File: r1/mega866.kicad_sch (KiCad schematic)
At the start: 18 parts, among them J1 ZSM1-SM1, J2 ZSM1-SM2

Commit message: schematic draft
Signed-off-by: John McMaster <johndmcmaster@gmail.com>
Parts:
- removed J? (x5): tl866_dip40, symbol mega866:tl866_dip40
- removed R?: 100k, Resistor_SMD:R_0603_1608Metric, symbol Device:R
- added J? (x4): tl866_dip40, symbol mega866:tl866_dip40
- added J? (x2): Conn_01x02_Male, symbol Connector:Conn_01x02_Male
- added Q? (x2): 2N7002, Package_TO_SOT_SMD:SOT-23, symbol Transistor_FET:2N7002
- added Q?: BSS84, Package_TO_SOT_SMD:SOT-23, symbol Transistor_FET:IRF7606PBF
- added R? (x4): NOLOAD, Resistor_SMD:R_0603_1608Metric, symbol Device:R
- added R? (x10): 0, Resistor_SMD:R_0603_1608Metric, symbol Device:R
- added R? (x3): 4.7k, Resistor_SMD:R_0603_1608Metric, symbol Device:R
- added R?: 100k, Resistor_SMD:R_0603_1608Metric, symbol Device:R
- added R? (x2): 47k, Resistor_SMD:R_0603_1608Metric, symbol Device:R
- added U?: Pico, MCU_RaspberryPi_and_Boards:RPi_Pico_SMD_TH, symbol MCU_RaspberryPi_and_Boards:Pico
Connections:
- net BPM_SR_CLK: now also U?.20 (GPIO15)
- net BPM_SR_D: now also U?.19 (GPIO14)
- net G001: now also J?.1
- net G002: now also J?.21
- net G003: now also J?.40
- net G004: now also J?.20
- net G005: now also J?.2
- net G006: now also J?.22
- net G007: now also J?.39
- net G008: now also J?.19
- net G009: now also J?.3
- net G010: now also J?.23
- net G011: now also J?.38
- net G012: now also J?.18
- net G013: now also J?.4
- net G014: now also J?.24
- net G015: now also J?.37
- net G016: now also J?.17
- net G017: now also J?.5
- net G018: now also J?.25
- net G019: now also J?.36
- net G020: now also J?.16
- net G021: now also J?.6
- net G022: now also J?.26
- net G023: now also J?.35
- net G024: now also J?.15
- net G025: now also J?.7
- net G026: now also J?.27
- net G027: now also J?.34
- net G028: now also J?.14
- net G029: now also J?.8
- net G030: now also J?.28
- net G031: now also J?.33
- net G032: now also J?.13
- net G033: now also J?.9, R?.1
- net G034: now also J?.29
- net G035: now also J?.32
- net G036: now also J?.12
- net G037: now also J?.10, R?.1
- net G038: now also J?.30
- net G039: now also J?.31, R?.1
- net G040: now also J?.11
- net G041: now also J?.11, R?.1
- net G042: now also J?.31
- net G043: now also J?.30, Q?.3 (D), R?.1
- net G044: now also J?.10
- net G045: now also J?.12, R?.1
- net G046: now also J?.32
- net G047: now also J?.29
- net G048: now also J?.9
- net G049: now also J?.13
- net G050: now also J?.33
- net G051: now also J?.28
- net G052: now also J?.8
- net G053: now also J?.14
- net G054: now also J?.34
- net G055: now also J?.27
- net G056: now also J?.7
- net G057: now also J?.15
- net G058: now also J?.35
- net G059: now also J?.26
- net G060: now also J?.6
- net G061: now also J?.16
- net G062: now also J?.36
- net G063: now also J?.25
- net G064: now also J?.5
- net G065: now also J?.17
- net G066: now also J?.37
- net G067: now also J?.24
- net G068: now also J?.4
- net G069: now also J?.18
- net G070: now also J?.38
- net G071: now also J?.23
- net G072: now also J?.3
- net G073: now also J?.19
- net G074: now also J?.39
- net G075: now also J?.22
- net G076: now also J?.2
- net G077: now also J?.20
- net G078: now also J?.40
- net G079: now also J?.21
- net G080: now also J?.1
- net G081: now also J?.1
- net G082: now also J?.21
- net G083: now also J?.40
- net G084: now also J?.20
- net G085: now also J?.2
- net G086: now also J?.22
- net G087: now also J?.39
- net G088: now also J?.19
- net G089: now also J?.3
- net G090: now also J?.23
- net G091: now also J?.38
- net G092: now also J?.18
- net G093: now also J?.4
- net G094: now also J?.24
- net G095: now also J?.37
- net G096: now also J?.17
- net G097: now also J?.5
- net G098: now also J?.25
- net G099: now also J?.36
- net G100: now also J?.16
- net G101: now also J?.6
- net G102: now also J?.26
- net G103: now also J?.35
- net G104: now also J?.15
- net G105: now also J?.7
- net G106: now also J?.27
- net G107: now also J?.34
- net G108: now also J?.14
- net G109: now also J?.8
- net G110: now also J?.28
- net G111: now also J?.33
- net G112: now also J?.13
- net G113: now also J?.9
- net G114: now also J?.29
- net G115: now also J?.32
- net G116: now also J?.12
- net G117: now also J?.10
- net G118: now also J?.30
- net G119: now also J?.31
- net G120: now also J?.11
- net G121: now also J?.11
- net G122: now also J?.31
- net G123: now also J?.30
- net G124: now also J?.10
- net G125: now also J?.12
- net G126: now also J?.32
- net G127: now also J?.29
- net G128: now also J?.9
- net G129: now also J?.13
- net G130: now also J?.33
- net G131: now also J?.28
- net G132: now also J?.8
- net G133: now also J?.14
- net G134: now also J?.34
- net G135: now also J?.27
- net G136: now also J?.7
- net G137: now also J?.15
- net G138: now also J?.35
- net G139: now also J?.26
- net G140: now also J?.6
- net G141: now also J?.16
- net G142: now also J?.36
- net G143: now also J?.25
- net G144: now also J?.5
- net G145: now also J?.17
- net G146: now also J?.37
- net G147: now also J?.24
- net G148: now also J?.4
- net G149: now also J?.18
- net G150: now also J?.38
- net G151: now also J?.23
- net G152: now also J?.3
- net G153: now also J?.19
- net G154: now also J?.39
- net G155: now also J?.22
- net G156: now also J?.2
- net G157: now also J?.20
- net G158: now also J?.40
- net G159: now also J?.21
- net G160: now also J?.1
- net GND: now also Q?.2 (S), Q?.2 (S), R?.1, R?.1, R?.2, U?.13 (GND), U?.18 (GND), U?.23 (GND), U?.28 (GND), U?.3 (GND), U?.33 (AGND), U?.38 (GND), U?.8 (GND)
- net LED1: now also U?.21 (GPIO16)
- net LED2: now also U?.22 (GPIO17)
- net SM_DET: now also R?.2, U?.24 (GPIO18)
- net VCC: now also J?.2 (Pin_2), U?.39 (VSYS)
- net SM2_C3: now reaches J2.C3 (RFU)
- net SM2_C3: now also R?.1
- net COILP: now reaches J2.C4 (RFU)
- net COILP: now also Q?.5 (D), Q?.6 (D), Q?.7 (D), Q?.8 (D)
- net at J1.C3 (I2C_SDA): now also R?.2, R?.2
- net at J1.C4 (I2C_SCL): now also R?.1, R?.1
- net SM1_C5: now reaches J1.C5 (RFU)
- net SM1_C5: now also R?.1
- net P2R: now reaches J1.A30 (RFU)
- net P2R: now also J?.1 (Pin_1)
- net SM2_A5: now reaches J2.A5 (RFU)
- net SM2_A5: now also R?.1
- new net: R?.2, U?.31 (GPIO26_ADC0)
- new net: R?.2, U?.29 (GPIO22)
- new net: R?.2, U?.27 (GPIO21)
- new net: Q?.3 (D), Q?.4 (G), R?.1
- new net: J?.1 (Pin_1), Q?.1 (S), Q?.2 (S), Q?.3 (S), R?.2
- new net +3V3: R?.1, R?.1
- new net COIL_EN: Q?.1 (G), Q?.1 (G), R?.2, U?.25 (GPIO19)
- new net COIL_GPIO: J?.2 (Pin_2), U?.26 (GPIO20)
- new net EEPROM CLK: U?.4 (GPIO2)
- new net EEPROM CS: R?.1, U?.2 (GPIO1)
- new net EEPROM DI: U?.5 (GPIO3)
- new net EEPROM DO: U?.1 (GPIO0)
- new net G033_GPIO: R?.2, U?.9 (GPIO6)
- new net G037_GPIO: R?.2, U?.10 (GPIO7)
- new net G039_GPIO: R?.2, U?.11 (GPIO8)
- new net G041_GPIO: R?.2, U?.12 (GPIO9)
- new net G043_GPIO: R?.2, U?.14 (GPIO10)
- new net G045_GPIO: R?.2, U?.15 (GPIO11)
- new net I2C SCL: R?.1, R?.2, U?.7 (GPIO5)
- new net I2C SDA: R?.2, R?.2, U?.6 (GPIO4)
- new net SM2_C5: R?.1
- new net UART1: R?.2, U?.16 (GPIO12)
- new net UART2: R?.1, U?.17 (GPIO13)
- no-connect marks 10 -> 9
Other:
- note added: "3.3V to 5V level translation"
- note added: "A7 COILN"
- note added: "Although we could just switch COILN, don't apply power until we have a compatible connection"
- note added: "Considered TL866 for misc GPIO, but use RP2040 since easier to get and consistent with zscn"
- note added: "Following pins were connected on SM48D: -SM2.A12 (G033): G015 -SM2.A10 (G037): G019 -SM2.A09 (G039): G023 -SM2.A08 (G041): G027 Provide a way to test connections Add a few extra in case more are used that I don't know about"
- note added: "Give some flexibility for other voltage Bridge / jumper if unused"
- note added: "RFU: UART"
- note added: "SM48D relay control When COIL_EN is asserted, the SM will connect P2R to P2 Right circuit drives relay COILP (SM2.C4) Note COILN on G043 (SM2.A7) Add transistor here to make atomic, although we could probably toggle through TL866"
- note added: "Signal fed into SM's relay When closed, connects to P2 Intended for loopback testing?"
- note removed: "93C46B"
- note removed: "Misc GPIO w/ tl866 to keep things consistent? Otherwise rp2040"
- note removed: "VCC 3.3V or 5V probably ok"
- moved on the sheet: D?, J1A, J1B, J1C, J2A, J2B, J2C, R?

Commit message: fix erc errors
Signed-off-by: John McMaster <johndmcmaster@gmail.com>
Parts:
- removed J?: Conn_01x06_Male, symbol Connector:Conn_01x06_Male
- removed R?: 4.7k, Resistor_SMD:R_0603_1608Metric, symbol Device:R
- removed R?: 0, Resistor_SMD:R_0603_1608Metric, symbol Device:R
- added R4: 4.7k, Resistor_SMD:R_0603_1608Metric, symbol Device:R
- gave numbers to parts that had none: 37
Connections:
- net +3V3: now also R4.1
- net I2C SCL: now also R4.2
- no-connect marks 9 -> 31

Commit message: cleaner drc / fix errors
Signed-off-by: John McMaster <johndmcmaster@gmail.com>
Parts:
- D1, D2: footprint (none) -> LED_SMD:LED_0603_1608Metric
- J1: footprint zsm:5650470-5 -> TE_5650933-5; symbol zsm:ZSM1-SM1 -> mega866:ZSM1-SM1
- J10, J6, J7, J9: footprint (none) -> Connector_PinHeader_2.54mm:PinHeader_1x06_P2.54mm_Vertical
- J2: symbol zsm:ZSM1-SM2 -> mega866:ZSM1-SM2
- J5, J8: footprint (none) -> Connector_PinHeader_2.54mm:PinHeader_1x02_P2.54mm_Vertical
- R1, R2: footprint (none) -> Resistor_SMD:R_0603_1608Metric
- U1: footprint MCU_RaspberryPi_and_Boards:RPi_Pico_SMD_TH -> mega866:RPi_Pico_SMD_TH; symbol MCU_RaspberryPi_and_Boards:Pico -> mega866:Pico
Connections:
- net EE_CLK is gone; now on net EEPROM_CLK: J2.A3 (EE_CLK)
- net EE_CS is gone; now on net EEPROM_CS: J2.A4 (EE_CS)
- net EE_DI is gone; now on net EEPROM_DI: J2.A2 (EE_DI)
- net EE_DO is gone; now on net EEPROM_DO: J2.A1 (EE_DO)
- net EEPROM CLK renamed EEPROM_CLK
- net EEPROM CS renamed EEPROM_CS
- net EEPROM DI renamed EEPROM_DI
- net EEPROM DO renamed EEPROM_DO
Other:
- note added: "TODO: confirm these are actually 0.1 pitch"

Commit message: WIP
Signed-off-by: John McMaster <johndmcmaster@gmail.com>
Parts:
- removed J7, J9: Conn_01x06_Male, Connector_PinHeader_2.54mm:PinHeader_1x06_P2.54mm_Vertical, symbol Connector:Conn_01x06_Male
- removed Q1: BSS84, Package_TO_SOT_SMD:SOT-23, symbol Transistor_FET:IRF7606PBF
- added J4, J8: Conn_01x06_Male, Connector_PinHeader_2.54mm:PinHeader_1x06_P2.54mm_Vertical, symbol Connector:Conn_01x06_Male
- added Q1: BSS84, Package_TO_SOT_SMD:SOT-23, symbol Transistor_FET:BSS84
- J1: footprint TE_5650933-5 -> mega866:5650470-5
- J2: footprint zsm:5650470-5 -> mega866:5650470-5
- J3: footprint (none) -> mega866:tl866
- J5: renamed from J12; footprint (none) -> mega866:tl866
- J7: renamed from J4; footprint (none) -> mega866:tl866
- J9: renamed from J13; footprint (none) -> mega866:tl866
- renumbered J8 to J11, J5 to J12
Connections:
- net COILP: now also Q1.3 (D)
- net G082: now also J9.20; no longer J9.21
- net G084: now also J9.21; no longer J9.20
- net G086: now also J9.19; no longer J9.22
- net G088: now also J9.22; no longer J9.19
- net G090: now also J9.18; no longer J9.23
- net G092: now also J9.23; no longer J9.18
- net G094: now also J9.17; no longer J9.24
- net G096: now also J9.24; no longer J9.17
- net G098: now also J9.16; no longer J9.25
- net G100: now also J9.25; no longer J9.16
- net G102: now also J9.15; no longer J9.26
- net G104: now also J9.26; no longer J9.15
- net G106: now also J9.14; no longer J9.27
- net G108: now also J9.27; no longer J9.14
- net G110: now also J9.13; no longer J9.28
- net G112: now also J9.28; no longer J9.13
- net G114: now also J9.12; no longer J9.29
- net G116: now also J9.29; no longer J9.12
- net G118: now also J9.11; no longer J9.30
- net G120: now also J9.30; no longer J9.11
- net G122: now also J9.10; no longer J9.31
- net G124: now also J9.31; no longer J9.10
- net G126: now also J9.9; no longer J9.32
- net G128: now also J9.32; no longer J9.9
- net G130: now also J9.8; no longer J9.33
- net G132: now also J9.33; no longer J9.8
- net G134: now also J9.7; no longer J9.34
- net G136: now also J9.34; no longer J9.7
- net G138: now also J9.6; no longer J9.35
- net G140: now also J9.35; no longer J9.6
- net G142: now also J9.5; no longer J9.36
- net G144: now also J9.36; no longer J9.5
- net G146: now also J9.4; no longer J9.37
- net G148: now also J9.37; no longer J9.4
- net G150: now also J9.3; no longer J9.38
- net G152: now also J9.38; no longer J9.3
- net G154: now also J9.2; no longer J9.39
- net G156: now also J9.39; no longer J9.2
- net G158: now also J9.1; no longer J9.40
- net G160: now also J9.40; no longer J9.1
- net GND: now also J4.3 (Pin_3), J8.3 (Pin_3)
- net at Q2.3 (D), R3.1: now also Q1.1 (G)
- net at J11.1 (Pin_1), R3.2: now also Q1.2 (S)
- no-connect marks 31 -> 26
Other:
- moved on the sheet: J9

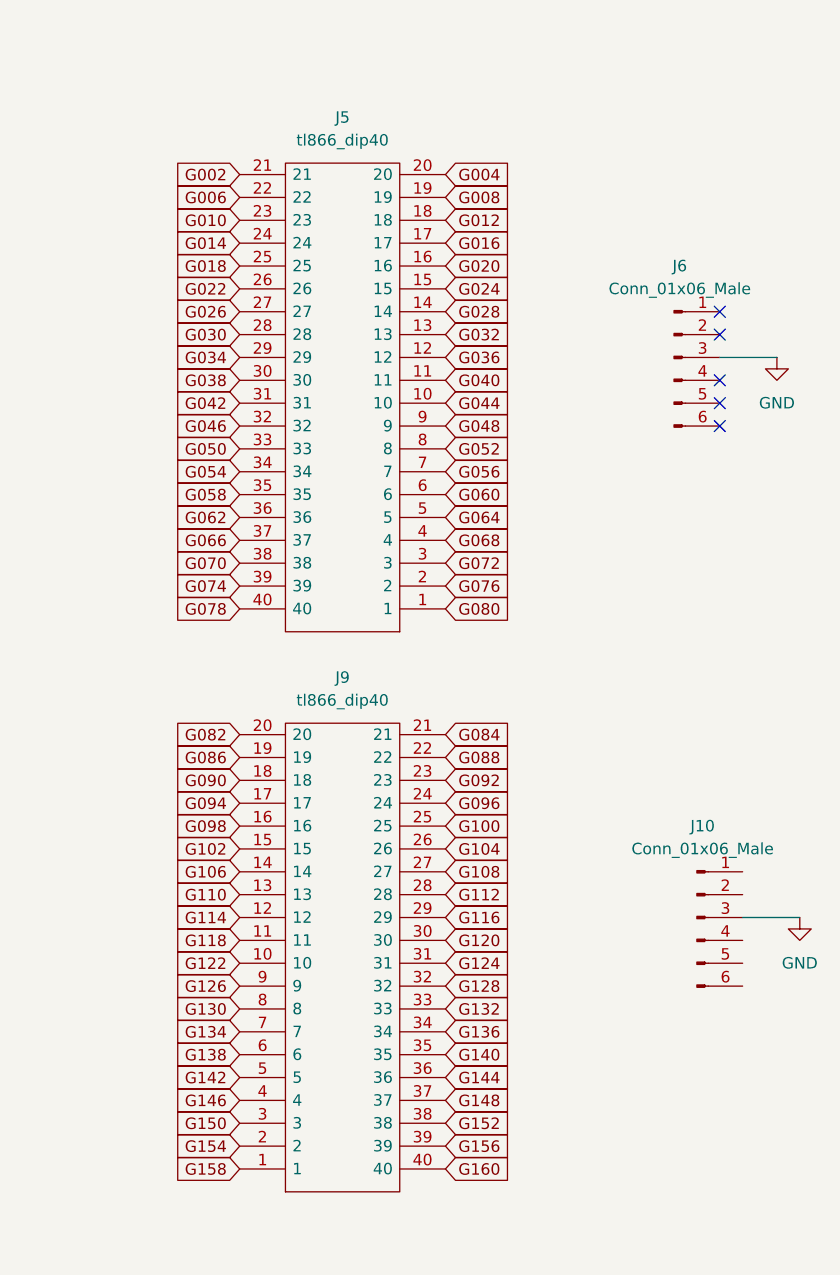
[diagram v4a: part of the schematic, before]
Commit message: reassign pins for easier routing
Signed-off-by: John McMaster <johndmcmaster@gmail.com>
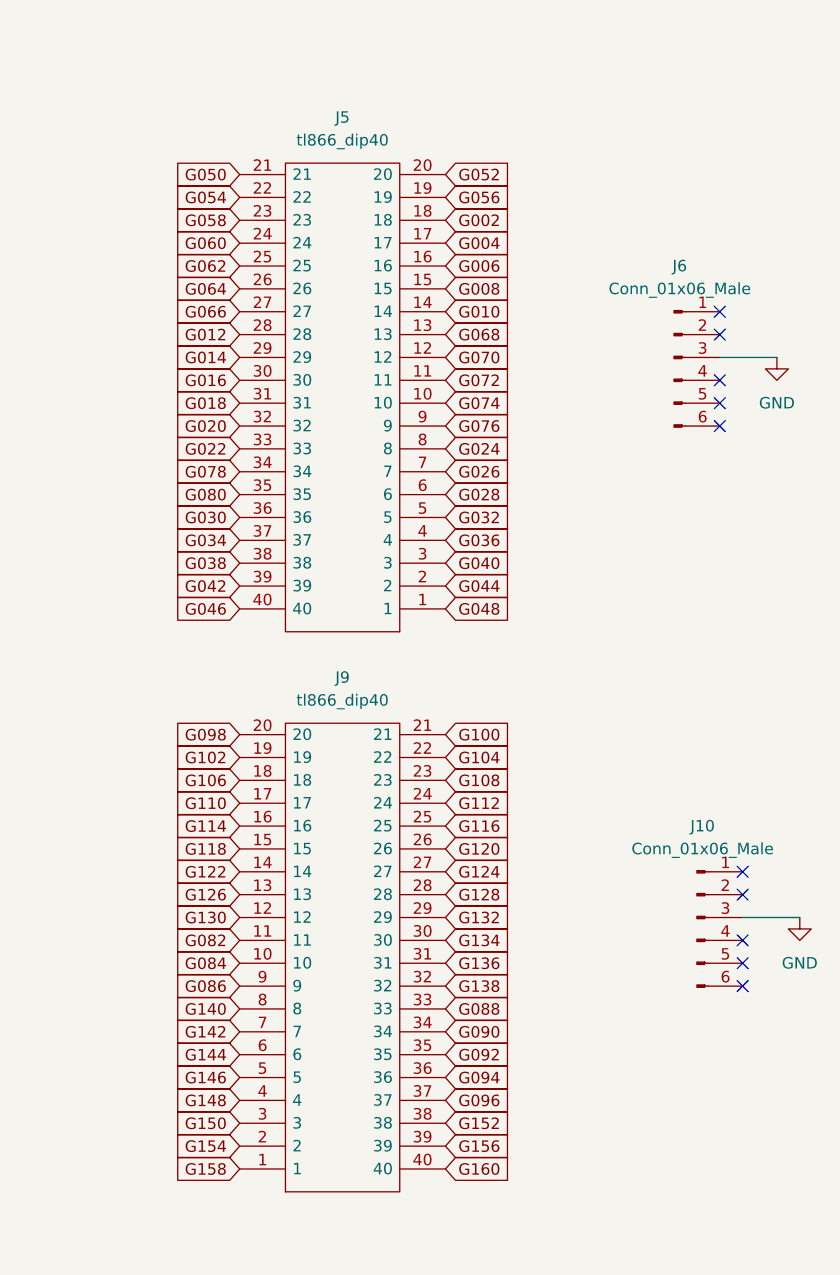
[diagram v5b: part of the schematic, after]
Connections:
- net G002: now also J5.18; no longer J5.21
- net G004: now also J5.17; no longer J5.20
- net G006: now also J5.16; no longer J5.22
- net G008: now also J5.15; no longer J5.19
- net G010: now also J5.14; no longer J5.23
- net G012: now also J5.28; no longer J5.18
- net G014: now also J5.29; no longer J5.24
- net G016: now also J5.30; no longer J5.17
- net G018: now also J5.31; no longer J5.25
- net G020: now also J5.32; no longer J5.16
- net G022: now also J5.33; no longer J5.26
- net G024: now also J5.8; no longer J5.15
- net G026: now also J5.7; no longer J5.27
- net G028: now also J5.6; no longer J5.14
- net G030: now also J5.36; no longer J5.28
- net G032: now also J5.5; no longer J5.13
- net G034: now also J5.37; no longer J5.29
- net G036: now also J5.4; no longer J5.12
- net G038: now also J5.38; no longer J5.30
- net G040: now also J5.3; no longer J5.11
- net G042: now also J5.39; no longer J5.31
- net G044: now also J5.2; no longer J5.10
- net G046: now also J5.40; no longer J5.32
- net G048: now also J5.1; no longer J5.9
- net G050: now also J5.21; no longer J5.33
- net G052: now also J5.20; no longer J5.8
- net G054: now also J5.22; no longer J5.34
- net G056: now also J5.19; no longer J5.7
- net G058: now also J5.23; no longer J5.35
- net G060: now also J5.24; no longer J5.6
- net G062: now also J5.25; no longer J5.36
- net G064: now also J5.26; no longer J5.5
- net G066: now also J5.27; no longer J5.37
- net G068: now also J5.13; no longer J5.4
- net G070: now also J5.12; no longer J5.38
- net G072: now also J5.11; no longer J5.3
- net G074: now also J5.10; no longer J5.39
- net G076: now also J5.9; no longer J5.2
- net G078: now also J5.34; no longer J5.40
- net G080: now also J5.35; no longer J5.1
- net G082: now also J9.11; no longer J9.20
- net G084: now also J9.10; no longer J9.21
- net G086: now also J9.9; no longer J9.19
- net G088: now also J9.33; no longer J9.22
- net G090: now also J9.34; no longer J9.18
- net G092: now also J9.35; no longer J9.23
- net G094: now also J9.36; no longer J9.17
- net G096: now also J9.37; no longer J9.24
- net G098: now also J9.20; no longer J9.16
- net G100: now also J9.21; no longer J9.25
- net G102: now also J9.19; no longer J9.15
- net G104: now also J9.22; no longer J9.26
- net G106: now also J9.18; no longer J9.14
- net G108: now also J9.23; no longer J9.27
- net G110: now also J9.17; no longer J9.13
- net G112: now also J9.24; no longer J9.28
- net G114: now also J9.16; no longer J9.12
- net G116: now also J9.25; no longer J9.29
- net G118: now also J9.15; no longer J9.11
- net G120: now also J9.26; no longer J9.30
- net G122: now also J9.14; no longer J9.10
- net G124: now also J9.27; no longer J9.31
- net G126: now also J9.13; no longer J9.9
- net G128: now also J9.28; no longer J9.32
- net G130: now also J9.12; no longer J9.8
- net G132: now also J9.29; no longer J9.33
- net G134: now also J9.30; no longer J9.7
- net G136: now also J9.31; no longer J9.34
- net G138: now also J9.32; no longer J9.6
- net G140: now also J9.8; no longer J9.35
- net G142: now also J9.7; no longer J9.5
- net G144: now also J9.6; no longer J9.36
- net G146: now also J9.5; no longer J9.4
- net G148: now also J9.4; no longer J9.37
- no-connect marks 26 -> 31

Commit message: release candidate
Signed-off-by: John McMaster <johndmcmaster@gmail.com>
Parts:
- added R16, R24: 0, Resistor_SMD:R_0603_1608Metric, symbol Device:R
- renumbered R23 to R18, R22 to R19, R21 to R20, R20 to R21, R19 to R22, R18 to R23
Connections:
- net BPM_SR_CLK: now also R16.1; no longer J1.C1 (RFU)
- net BPM_SR_D: now also R24.1; no longer J1.C2 (RFU)
- net G001: now also J3.3; no longer J3.1
- net G003: now also J3.4; no longer J3.40
- net G005: now also J3.5; no longer J3.2
- net G007: now also J3.6; no longer J3.39
- net G009: now also J3.7; no longer J3.3
- net G011: now also J3.33; no longer J3.38
- net G013: now also J3.32; no longer J3.4
- net G015: now also J3.31; no longer J3.37
- net G017: now also J3.30; no longer J3.5
- net G019: now also J3.29; no longer J3.36
- net G021: now also J3.28; no longer J3.6
- net G023: now also J3.13; no longer J3.35
- net G025: now also J3.14; no longer J3.7
- net G027: now also J3.15; no longer J3.34
- net G029: now also J3.25; no longer J3.8
- net G031: now also J3.16; no longer J3.33
- net G033: now also J3.24; no longer J3.9
- net G033_GPIO: now also U1.15 (GPIO11); no longer U1.9 (GPIO6)
- net G035: now also J3.17; no longer J3.32
- net G037: now also J3.23; no longer J3.10
- net G037_GPIO: now also U1.14 (GPIO10); no longer U1.10 (GPIO7)
- net G039: now also J3.18; no longer J3.31
- net G039_GPIO: now also U1.12 (GPIO9); no longer U1.11 (GPIO8)
- net G041: now also J3.22; no longer J3.11
- net G041_GPIO: now also U1.11 (GPIO8); no longer U1.12 (GPIO9)
- net G043: now also J3.19; no longer J3.30
- net G043_GPIO: now also U1.10 (GPIO7); no longer U1.14 (GPIO10)
- net G045: now also J3.21; no longer J3.12
- net G045_GPIO: now also U1.9 (GPIO6); no longer U1.15 (GPIO11)
- net G047: now also J3.20; no longer J3.29
- net G049: now also J3.40; no longer J3.13
- net G051: now also J3.1; no longer J3.28
- net G053: now also J3.39; no longer J3.14
- net G055: now also J3.2; no longer J3.27
- net G057: now also J3.38; no longer J3.15
- net G059: now also J3.37; no longer J3.26
- net G061: now also J3.36; no longer J3.16
- net G063: now also J3.35; no longer J3.25
- net G065: now also J3.34; no longer J3.17
- net G067: now also J3.8; no longer J3.24
- net G069: now also J3.9; no longer J3.18
- net G071: now also J3.10; no longer J3.23
- net G073: now also J3.11; no longer J3.19
- net G075: now also J3.12; no longer J3.22
- net G077: now also J3.27; no longer J3.20
- net G079: now also J3.26; no longer J3.21
- net G081: now also J7.31; no longer J7.1
- net G082: now also J9.30; no longer J9.11
- net G083: now also J7.30; no longer J7.40
- net G084: now also J9.31; no longer J9.10
- net G085: now also J7.29; no longer J7.2
- net G086: now also J9.32; no longer J9.9
- net G087: now also J7.14; no longer J7.39
- net G088: now also J9.7; no longer J9.33
- net G089: now also J7.15; no longer J7.3
- net G090: now also J9.6; no longer J9.34
- net G091: now also J7.16; no longer J7.38
- net G092: now also J9.5; no longer J9.35
- net G093: now also J7.17; no longer J7.4
- net G094: now also J9.4; no longer J9.36
- net G095: now also J7.18; no longer J7.37
- net G096: now also J9.3; no longer J9.37
- net G097: now also J7.1; no longer J7.5
- net G099: now also J7.40; no longer J7.36
- net G101: now also J7.2; no longer J7.6
- net G103: now also J7.39; no longer J7.35
- net G105: now also J7.3; no longer J7.7
- net G107: now also J7.38; no longer J7.34
- net G109: now also J7.4; no longer J7.8
- net G111: now also J7.37; no longer J7.33
- net G113: now also J7.5; no longer J7.9
- net G115: now also J7.36; no longer J7.32
- net G117: now also J7.6; no longer J7.10
- net G119: now also J7.35; no longer J7.31
- net G121: now also J7.7; no longer J7.11
- net G123: now also J7.34; no longer J7.30
- net G125: now also J7.8; no longer J7.12
- net G127: now also J7.33; no longer J7.29
- net G129: now also J7.9; no longer J7.13
- net G131: now also J7.32; no longer J7.28
- net G133: now also J7.10; no longer J7.14
- net G134: now also J9.11; no longer J9.30
- net G135: now also J7.11; no longer J7.27
- net G136: now also J9.10; no longer J9.31
- net G137: now also J7.12; no longer J7.15
- net G138: now also J9.9; no longer J9.32
- net G139: now also J7.13; no longer J7.26
- net G141: now also J7.28; no longer J7.16
- net G142: now also J9.33; no longer J9.7
- net G143: now also J7.27; no longer J7.25
- net G144: now also J9.34; no longer J9.6
- net G145: now also J7.26; no longer J7.17
- net G146: now also J9.35; no longer J9.5
- net G147: now also J7.25; no longer J7.24
- net G148: now also J9.36; no longer J9.4
- net G149: now also J7.24; no longer J7.18
- net G150: now also J9.37; no longer J9.3
- new net: J1.C1 (RFU), R16.2
- new net: J1.C2 (RFU), R24.2
